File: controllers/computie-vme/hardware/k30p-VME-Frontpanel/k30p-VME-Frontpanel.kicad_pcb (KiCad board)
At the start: 2 copper layers, 19.9 x 128.5 mm, 11 parts

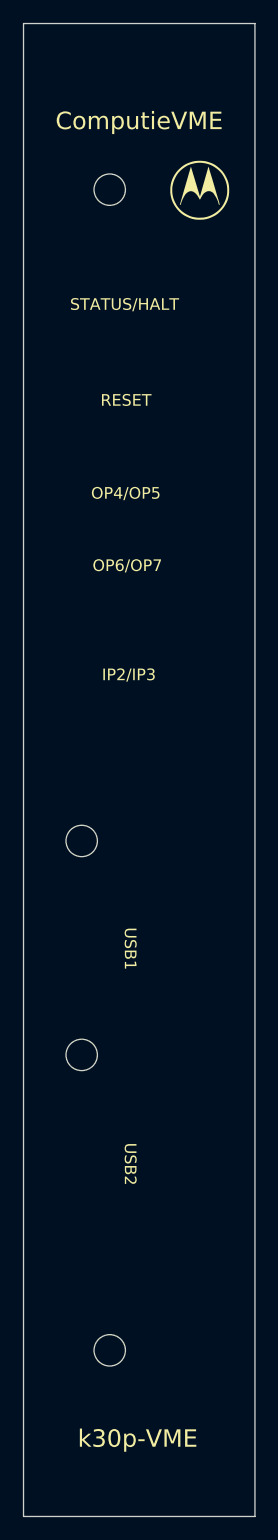
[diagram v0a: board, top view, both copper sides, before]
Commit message: Added MemBird - Woodcock (16-bit VME memory card)
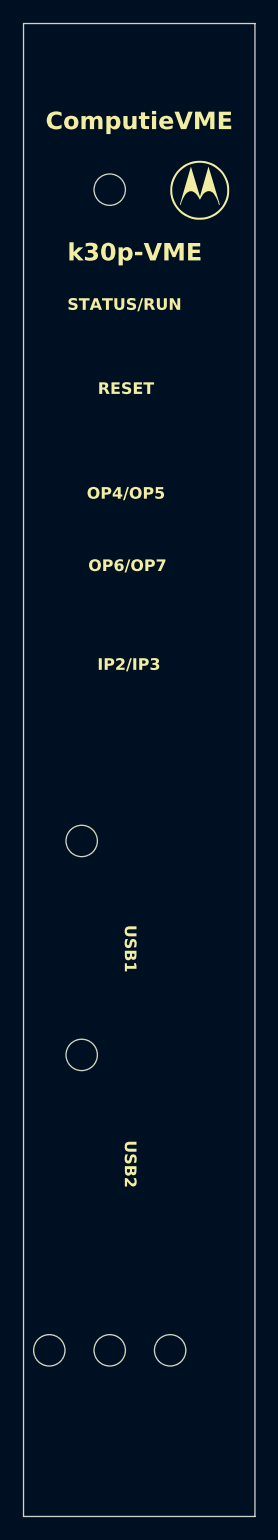
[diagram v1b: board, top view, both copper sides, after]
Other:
- board text added: "STATUS/RUN"
- board text removed: "STATUS/HALT"
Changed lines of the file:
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@@
 			(outputformat 1)
 			(mirror no)
-			(drillshape 1)
+			(drillshape 0)
 			(scaleselection 1)
 			(outputdirectory "")
@@
 		(pad "" np_thru_hole oval
 			(at 0 0)
-			(size 9 3.3)
-			(drill oval 9 3.3)
+			(size 9 4.5)
+			(drill oval 9 4.5)
 			(layers "F&B.Cu" "*.Mask")
 		)
@@
 		)
 		(pad "" np_thru_hole circle
+			(at 2.42 114.2)
+			(size 2.7 2.7)
+			(drill 2.7)
+			(layers "F&B.Cu" "*.Mask")
+		)
+		(pad "" np_thru_hole circle
 			(at 7.62 14.3)
 			(size 2.7 2.7)
@@
 		(pad "" np_thru_hole circle
 			(at 7.62 114.2)
+			(size 2.7 2.7)
+			(drill 2.7)
+			(layers "F&B.Cu" "*.Mask")
+		)
+		(pad "" np_thru_hole circle
+			(at 12.82 114.2)
 			(size 2.7 2.7)
 			(drill 2.7)
@@
 		(pad "" np_thru_hole oval
 			(at 0 0)
-			(size 9 3.3)
-			(drill oval 9 3.3)
+			(size 9 4.5)
+			(drill oval 9 4.5)
 			(layers "F&B.Cu" "*.Mask")
 		)
@@
 	)
 	(gr_line
-		(start 80.264 65.0494)
-		(end 87.039 65.0494)
-		(stroke
-			(width 0.1)
-			(type default)
-		)
-		(layer "F.Fab")
-	)
-	(gr_line
-		(start 80.2386 73.2282)
-		(end 87.0136 73.2282)
-		(stroke
-			(width 0.1)
-			(type default)
-		)
-		(layer "F.Fab")
-	)
-	(gr_line
 		(start 83.82 52.4)
 		(end 83.82 152.3)
@@
 			(font
 				(size 1 1)
-				(thickness 0.15)
+				(thickness 0.2)
+				(bold yes)
 			)
 			(justify bottom)
@@
 	)
 	(gr_text "RESET"
-		(at 85.217 71.12 0)
+		(at 85.217 70.104 0)
 		(layer "F.SilkS")
 		(effects
 			(font
 				(size 1 1)
-				(thickness 0.15)
+				(thickness 0.2)
+				(bold yes)
 			)
 			(justify bottom)
@@
 	)
 	(gr_text "IP2/IP3"
-		(at 85.471 94.742 0)
+		(at 85.471 93.853 0)
 		(layer "F.SilkS")
 		(effects
 			(font
 				(size 1 1)
-				(thickness 0.15)
+				(thickness 0.2)
+				(bold yes)
 			)
 			(justify bottom)
@@
 	)
 	(gr_text "k30p-VME"
-		(at 86.233 160.782 0)
+		(at 85.979 58.674 0)
 		(layer "F.SilkS")
 		(effects
 			(font
 				(size 1.5 1.5)
-				(thickness 0.2)
+				(thickness 0.3)
+				(bold yes)
 			)
 			(justify bottom)
@@
 			(font
 				(size 1.5 1.5)
-				(thickness 0.2)
+				(thickness 0.3)
+				(bold yes)
 			)
 			(justify bottom)
@@
 			(font
 				(size 1 1)
-				(thickness 0.15)
+				(thickness 0.2)
+				(bold yes)
 			)
 			(justify bottom)
@@
 			(font
 				(size 1 1)
-				(thickness 0.15)
+				(thickness 0.2)
+				(bold yes)
 			)
 			(justify bottom)
 		)
 	)
-	(gr_text "STATUS/HALT"
+	(gr_text "STATUS/RUN"
 		(at 85.09 62.865 0)
 		(layer "F.SilkS")
@@
 			(font
 				(size 1 1)
-				(thickness 0.15)
+				(thickness 0.2)
+				(bold yes)
 			)
 			(justify bottom)
@@
 			(font
 				(size 1 1)
-				(thickness 0.15)
+				(thickness 0.2)
+				(bold yes)
 			)
 			(justify bottom)

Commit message: k30p-VME rev.1, MemBird Woodcock rev.1, and frontpanels
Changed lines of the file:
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@@
 		(pad "" np_thru_hole oval
 			(at -0.166 0.794 90)
-			(size 11 5)
-			(drill oval 11 5)
+			(size 12 7)
+			(drill oval 12 7)
 			(layers "F&B.Cu" "*.Mask")
 		)
@@
 		)
 		(fp_rect
-			(start 2.5 106.4)
-			(end 12.7 117.5)
+			(start 2.52 11)
+			(end 12.72 22.1)
 			(stroke
 				(width 0.12)
@@
 		)
 		(fp_rect
-			(start 2.52 11)
-			(end 12.72 22.1)
+			(start 2.52 106.4)
+			(end 12.72 117.5)
 			(stroke
 				(width 0.12)
@@
 		(pad "" np_thru_hole oval
 			(at 0.634 -0.603 90)
-			(size 11 5)
-			(drill oval 11 5)
+			(size 12 7)
+			(drill oval 12 7)
 			(layers "F&B.Cu" "*.Mask")
 		)
@@
 	)
 	(gr_text "USB1"
-		(at 85 117.73 270)
+		(at 86.106 117.73 270)
 		(layer "F.SilkS")
 		(effects
@@
 	)
 	(gr_text "USB2"
-		(at 85 136.271 270)
+		(at 86.106 136.271 270)
 		(layer "F.SilkS")
 		(effects
